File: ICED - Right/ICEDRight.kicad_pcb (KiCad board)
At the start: 2 copper layers, 175.4 x 145 mm, 164 parts, among them P1 FLASH_HDR, P2 USBC, P3 CONN_17, P4 USB3_AFEMALE, Q1 TC1264, U1 MK20DX256VLH7, U2 IS31FL3731C, X1 CRYSTAL

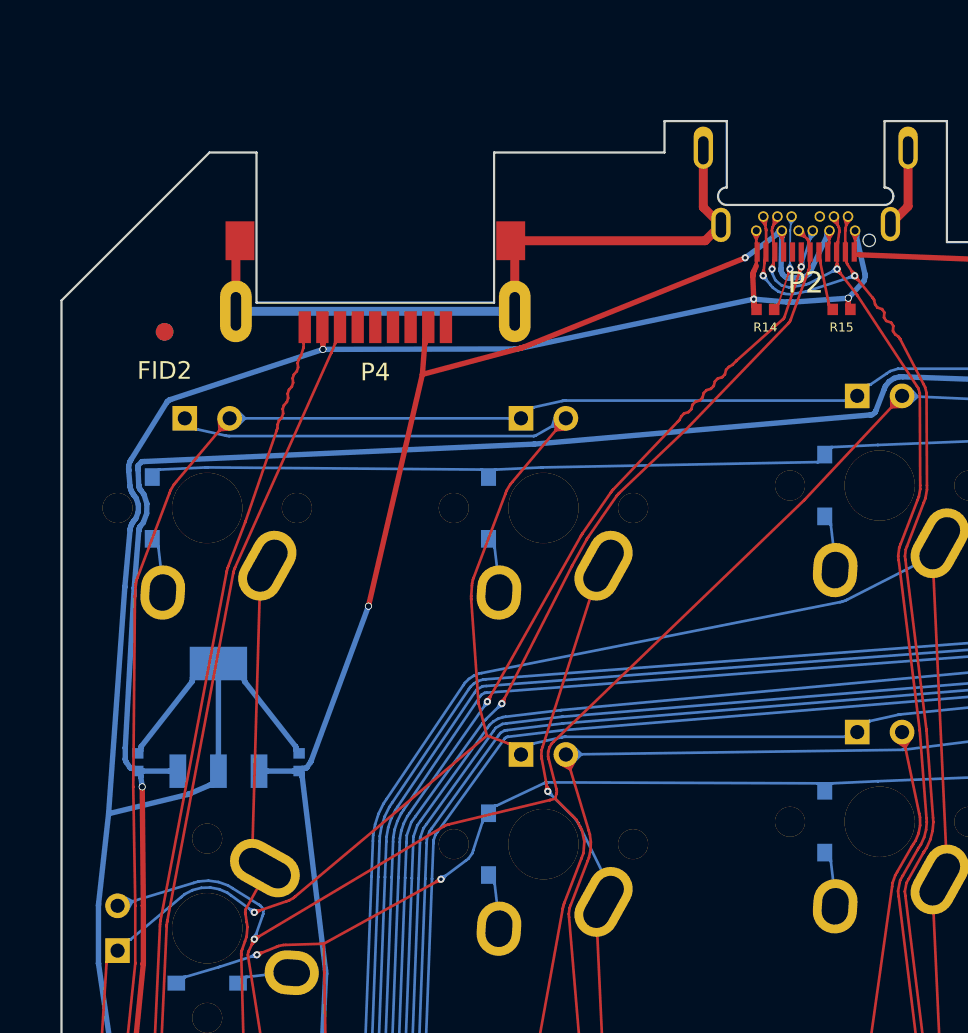
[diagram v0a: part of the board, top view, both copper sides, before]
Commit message: Update USB A connector
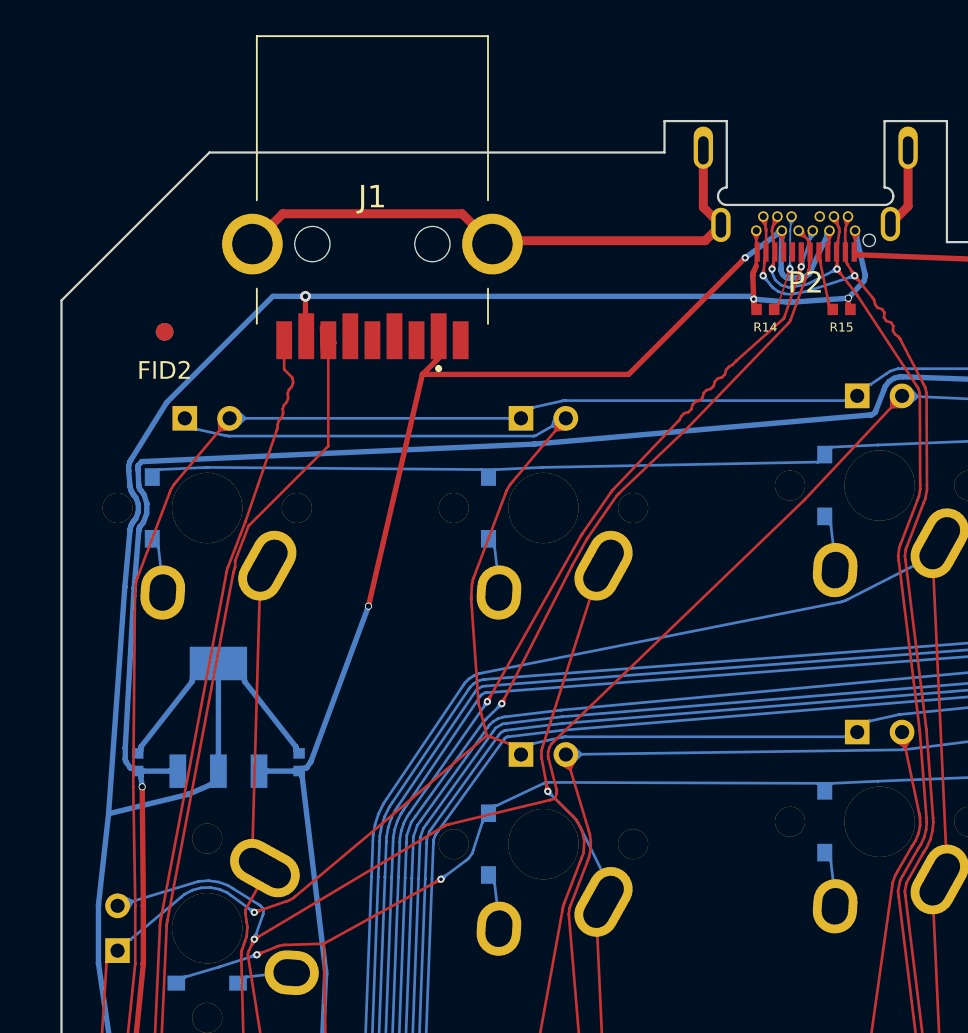
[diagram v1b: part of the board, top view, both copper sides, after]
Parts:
- removed IC_LOGO: , prettylib:IC_LOGO
- removed P4: USB3_AFEMALE, prettylib:USB3_AFEMALE_MOD
- added G***: LOGO, prettylib:dickbut, B.Cu at (184.7, 49.2)
- added J1: 692122030100, prettylib:692122030100, F.Cu at (81.8, 50.1)
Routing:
- net /GND: track 45.5 -> 37.7 mm
- net VSS: track 403.3 -> 407.6 mm
- net /mcu/RX0: track 159.8 -> 161.8 mm
- net +5V: track 211.7 -> 213.1 mm
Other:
- outline, holes or cut-outs redrawn
- board text added: "ICED-R Rev 1.3 Batch 01"
- board text removed: "ICED-R Rev 1.2b Batch __"
